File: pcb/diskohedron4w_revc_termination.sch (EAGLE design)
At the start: 64 parts

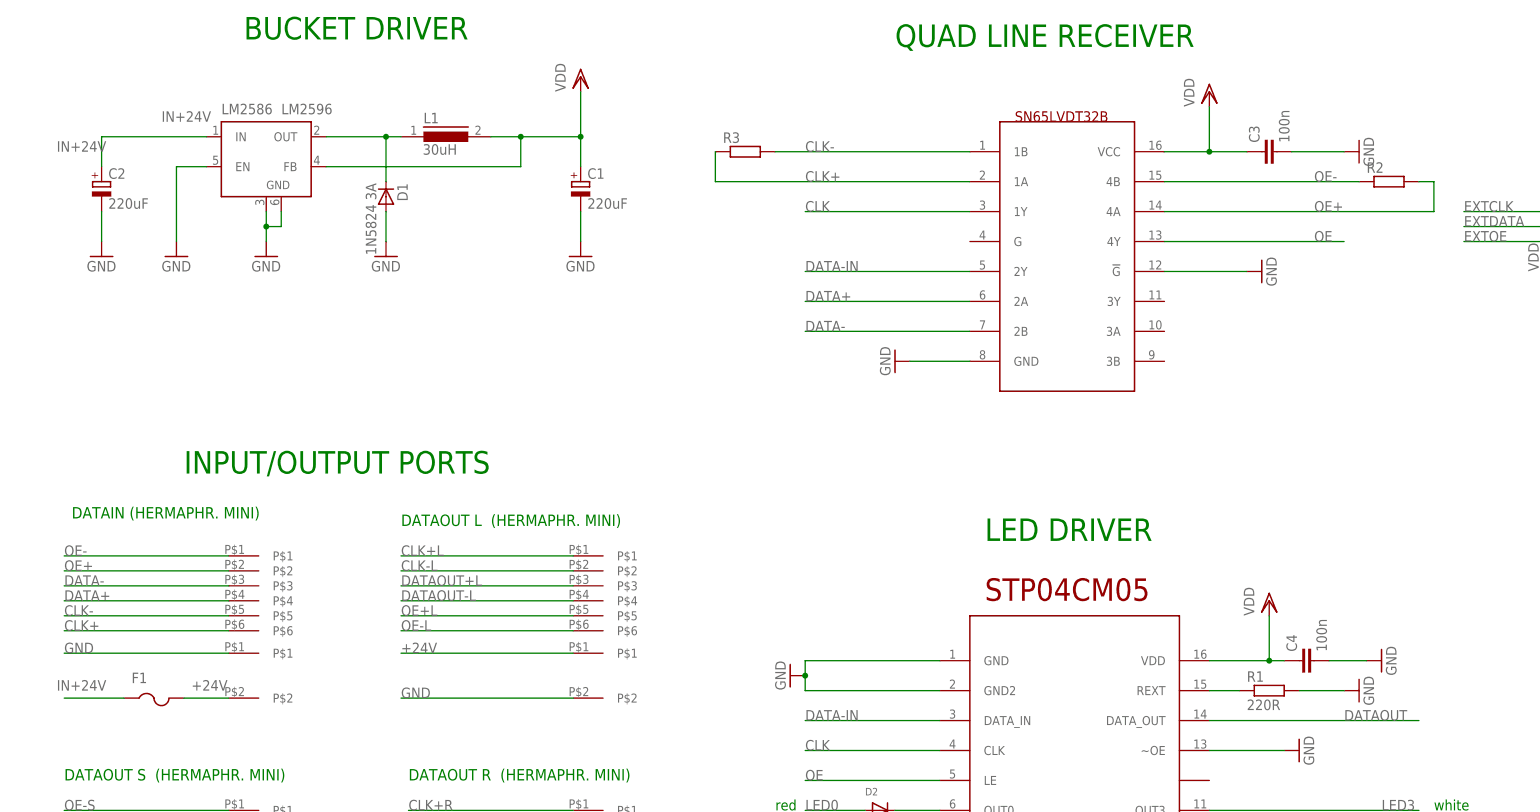
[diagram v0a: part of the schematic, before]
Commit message: added termination resistors for rev.c & d
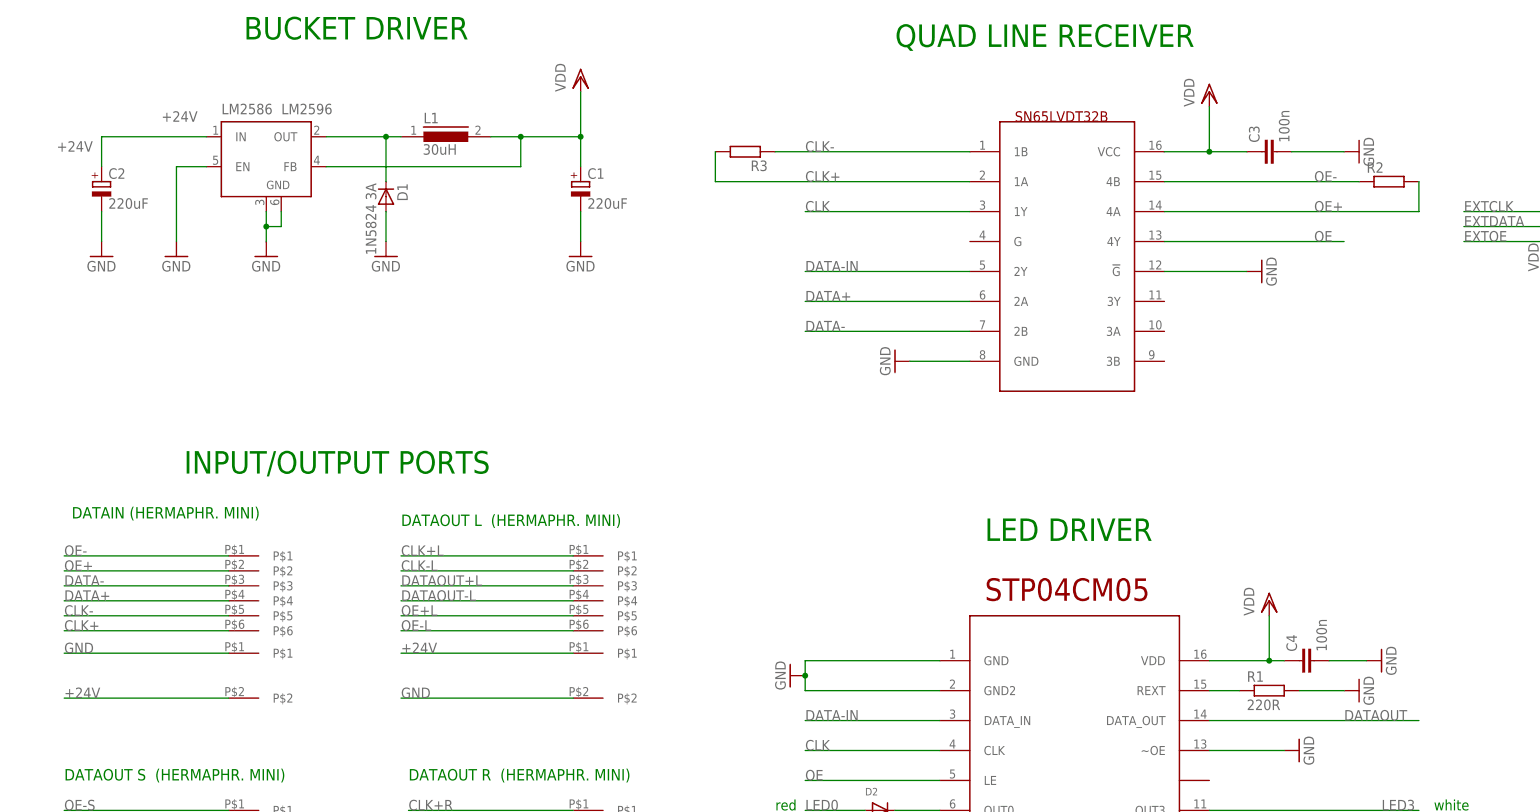
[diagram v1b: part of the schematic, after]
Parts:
- removed F1: (no value), adafruit:PTCFUSE-1812
- R2, R3: device rcl:R-EU_R0603 -> rcl:R-EU_R0402
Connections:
- removed net IN+24V: C2.+, F1.1, LM2586.IN
- net +24V: now also C2.+, LM2586.IN; no longer F1.2
- net CLK+: now also R3.2; no longer R3.1
- net CLK-: now also R3.1; no longer R3.2
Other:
- moved on the sheet: R3
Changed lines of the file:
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@@
 <grid distance="0.1" unitdist="inch" unit="inch" style="lines" multiple="1" display="no" altdistance="0.01" altunitdist="inch" altunit="inch"/>
 <layers>
-<layer number="1" name="Top" color="4" fill="1" visible="no" active="no"/>
-<layer number="16" name="Bottom" color="1" fill="1" visible="no" active="no"/>
-<layer number="17" name="Pads" color="2" fill="1" visible="no" active="no"/>
-<layer number="18" name="Vias" color="2" fill="1" visible="no" active="no"/>
-<layer number="19" name="Unrouted" color="6" fill="1" visible="no" active="no"/>
-<layer number="20" name="Dimension" color="15" fill="1" visible="no" active="no"/>
-<layer number="21" name="tPlace" color="7" fill="1" visible="no" active="no"/>
-<layer number="22" name="bPlace" color="7" fill="1" visible="no" active="no"/>
-<layer number="23" name="tOrigins" color="15" fill="1" visible="no" active="no"/>
-<layer number="24" name="bOrigins" color="15" fill="1" visible="no" active="no"/>
-<layer number="25" name="tNames" color="7" fill="1" visible="no" active="no"/>
-<layer number="26" name="bNames" color="7" fill="1" visible="no" active="no"/>
-<layer number="27" name="tValues" color="7" fill="1" visible="no" active="no"/>
-<layer number="28" name="bValues" color="7" fill="1" visible="no" active="no"/>
+<layer number="1" name="Top" color="4" fill="1" visible="yes" active="no"/>
+<layer number="16" name="Bottom" color="1" fill="1" visible="yes" active="no"/>
+<layer number="17" name="Pads" color="2" fill="1" visible="yes" active="no"/>
+<layer number="18" name="Vias" color="2" fill="1" visible="yes" active="no"/>
+<layer number="19" name="Unrouted" color="6" fill="1" visible="yes" active="no"/>
+<layer number="20" name="Dimension" color="15" fill="1" visible="yes" active="no"/>
+<layer number="21" name="tPlace" color="7" fill="1" visible="yes" active="no"/>
+<layer number="22" name="bPlace" color="7" fill="1" visible="yes" active="no"/>
+<layer number="23" name="tOrigins" color="15" fill="1" visible="yes" active="no"/>
+<layer number="24" name="bOrigins" color="15" fill="1" visible="yes" active="no"/>
+<layer number="25" name="tNames" color="7" fill="1" visible="yes" active="no"/>
+<layer number="26" name="bNames" color="7" fill="1" visible="yes" active="no"/>
+<layer number="27" name="tValues" color="7" fill="1" visible="yes" active="no"/>
+<layer number="28" name="bValues" color="7" fill="1" visible="yes" active="no"/>
 <layer number="29" name="tStop" color="7" fill="3" visible="no" active="no"/>
 <layer number="30" name="bStop" color="7" fill="6" visible="no" active="no"/>
@@
 <layer number="35" name="tGlue" color="7" fill="4" visible="no" active="no"/>
 <layer number="36" name="bGlue" color="7" fill="5" visible="no" active="no"/>
-<layer number="37" name="tTest" color="7" fill="1" visible="no" active="no"/>
-<layer number="38" name="bTest" color="7" fill="1" visible="no" active="no"/>
+<layer number="37" name="tTest" color="7" fill="1" visible="yes" active="no"/>
+<layer number="38" name="bTest" color="7" fill="1" visible="yes" active="no"/>
 <layer number="39" name="tKeepout" color="4" fill="11" visible="no" active="no"/>
 <layer number="40" name="bKeepout" color="1" fill="11" visible="no" active="no"/>
@@
 <layer number="44" name="Drills" color="7" fill="1" visible="no" active="no"/>
 <layer number="45" name="Holes" color="7" fill="1" visible="no" active="no"/>
-<layer number="46" name="Milling" color="3" fill="1" visible="no" active="no"/>
-<layer number="47" name="Measures" color="7" fill="1" visible="no" active="no"/>
-<layer number="48" name="Document" color="7" fill="1" visible="no" active="no"/>
-<layer number="49" name="Reference" color="7" fill="1" visible="no" active="no"/>
-<layer number="50" name="dxf" color="7" fill="1" visible="no" active="no"/>
-<layer number="51" name="tDocu" color="7" fill="1" visible="no" active="no"/>
-<layer number="52" name="bDocu" color="7" fill="1" visible="no" active="no"/>
-<layer number="53" name="tGND_GNDA" color="7" fill="1" visible="no" active="no"/>
-<layer number="54" name="bGND_GNDA" color="7" fill="1" visible="no" active="no"/>
-<layer number="56" name="wert" color="7" fill="1" visible="no" active="no"/>
-<layer number="57" name="tCAD" color="7" fill="1" visible="no" active="no"/>
+<layer number="46" name="Milling" color="3" fill="1" visible="yes" active="no"/>
+<layer number="47" name="Measures" color="7" fill="1" visible="yes" active="no"/>
+<layer number="48" name="Document" color="7" fill="1" visible="yes" active="no"/>
+<layer number="49" name="Reference" color="7" fill="1" visible="yes" active="no"/>
+<layer number="50" name="dxf" color="7" fill="1" visible="yes" active="no"/>
+<layer number="51" name="tDocu" color="7" fill="1" visible="yes" active="no"/>
+<layer number="52" name="bDocu" color="7" fill="1" visible="yes" active="no"/>
+<layer number="53" name="tGND_GNDA" color="7" fill="1" visible="yes" active="no"/>
+<layer number="54" name="bGND_GNDA" color="7" fill="1" visible="yes" active="no"/>
+<layer number="56" name="wert" color="7" fill="1" visible="yes" active="no"/>
+<layer number="57" name="tCAD" color="7" fill="1" visible="yes" active="no"/>
 <layer number="91" name="Nets" color="2" fill="1" visible="yes" active="yes"/>
 <layer number="92" name="Busses" color="1" fill="1" visible="yes" active="yes"/>
@@
 <part name="TP39" library="testpad" deviceset="TP" device="TP09SQ" value="TPTP09SQ"/>
 <part name="TP40" library="testpad" deviceset="TP" device="TP09SQ" value="TPTP09SQ"/>
-<part name="F1" library="adafruit" deviceset="PTCFUSE" device="-1812"/>
-<part name="R2" library="rcl" deviceset="R-EU_" device="R0603"/>
-<part name="R3" library="rcl" deviceset="R-EU_" device="R0603"/>
+<part name="R2" library="rcl" deviceset="R-EU_" device="R0402"/>
+<part name="R3" library="rcl" deviceset="R-EU_" device="R0402"/>
 </parts>
 <sheets>
@@
 <attribute name="TP_SIGNAL_NAME" x="39.37" y="31.75" size="1.778" layer="97" rot="R270"/>
 </instance>
-<instance part="F1" gate="G$1" x="44.45" y="123.19"/>
 <instance part="R2" gate="G$1" x="254" y="213.36"/>
-<instance part="R3" gate="G$1" x="144.78" y="218.44"/>
+<instance part="R3" gate="G$1" x="144.78" y="218.44" rot="R180"/>
 </instances>
 <busses>
@@
 <net name="+24V" class="0">
 <segment>
+<pinref part="C2" gate="G$1" pin="+"/>
+<label x="45.72" y="223.52" size="1.778" layer="95"/>
+<pinref part="LM2586" gate="G$1" pin="IN"/>
+<wire x1="53.34" y1="220.98" x2="35.56" y2="220.98" width="0.1524" layer="91"/>
+<label x="27.94" y="218.44" size="1.778" layer="95"/>
+<wire x1="35.56" y1="215.9" x2="35.56" y2="220.98" width="0.1524" layer="91"/>
+</segment>
+<segment>
 <pinref part="U$7" gate="G$1" pin="P$2"/>
-<wire x1="57.15" y1="125.73" x2="49.53" y2="125.73" width="0.1524" layer="91"/>
-<pinref part="F1" gate="G$1" pin="2"/>
-<label x="50.8" y="127" size="1.778" layer="95"/>
+<wire x1="29.21" y1="125.73" x2="57.15" y2="125.73" width="0.1524" layer="91"/>
+<label x="29.21" y="125.73" size="1.778" layer="95"/>
+</segment>
+<segment>
+<wire x1="115.57" y1="90.17" x2="87.63" y2="90.17" width="0.1524" layer="91"/>
+<label x="87.63" y="90.17" size="1.778" layer="95"/>
+<pinref part="U$6" gate="G$1" pin="P$1"/>
 </segment>
 <segment>
@@
 <pinref part="U$1" gate="G$1" pin="P$2"/>
 </segment>
-<segment>
-<wire x1="115.57" y1="90.17" x2="87.63" y2="90.17" width="0.1524" layer="91"/>
-<label x="87.63" y="90.17" size="1.778" layer="95"/>
-<pinref part="U$6" gate="G$1" pin="P$1"/>
-</segment>
 </net>
 <net name="CLK+" class="0">
@@
 <wire x1="182.88" y1="213.36" x2="139.7" y2="213.36" width="0.1524" layer="91"/>
 <label x="154.94" y="213.36" size="1.778" layer="95"/>
-<pinref part="R3" gate="G$1" pin="1"/>
-<wire x1="139.7" y1="213.36" x2="139.7" y2="218.44" width="0.1524" layer="91"/>
+<pinref part="R3" gate="G$1" pin="2"/>
+<wire x1="139.7" y1="218.44" x2="139.7" y2="213.36" width="0.1524" layer="91"/>
 </segment>
 <segment>
@@
 <wire x1="182.88" y1="218.44" x2="149.86" y2="218.44" width="0.1524" layer="91"/>
 <label x="154.94" y="218.44" size="1.778" layer="95"/>
-<pinref part="R3" gate="G$1" pin="2"/>
+<pinref part="R3" gate="G$1" pin="1"/>
 </segment>
 <segment>
@@
 <segment>
 <pinref part="4R" gate="G$1" pin="4A"/>
-<wire x1="215.9" y1="208.28" x2="261.62" y2="208.28" width="0.1524" layer="91"/>
+<wire x1="215.9" y1="208.28" x2="259.08" y2="208.28" width="0.1524" layer="91"/>
 <label x="241.3" y="208.28" size="1.778" layer="95"/>
 <pinref part="R2" gate="G$1" pin="2"/>
-<wire x1="259.08" y1="213.36" x2="261.62" y2="213.36" width="0.1524" layer="91"/>
-<wire x1="261.62" y1="213.36" x2="261.62" y2="208.28" width="0.1524" layer="91"/>
+<wire x1="259.08" y1="208.28" x2="259.08" y2="213.36" width="0.1524" layer="91"/>
 </segment>
 <segment>
@@
 </segment>
 </net>
-<net name="IN+24V" class="0">
-<segment>
-<pinref part="F1" gate="G$1" pin="1"/>
-<wire x1="39.37" y1="125.73" x2="29.21" y2="125.73" width="0.1524" layer="91"/>
-<label x="27.94" y="127" size="1.778" layer="95"/>
-</segment>
-<segment>
-<pinref part="C2" gate="G$1" pin="+"/>
-<label x="45.72" y="223.52" size="1.778" layer="95"/>
-<pinref part="LM2586" gate="G$1" pin="IN"/>
-<wire x1="53.34" y1="220.98" x2="35.56" y2="220.98" width="0.1524" layer="91"/>
-<label x="27.94" y="218.44" size="1.778" layer="95"/>
-<wire x1="35.56" y1="215.9" x2="35.56" y2="220.98" width="0.1524" layer="91"/>
-</segment>
-</net>
